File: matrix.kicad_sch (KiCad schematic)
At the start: 122 parts, among them SW1 esc, SW10 9, SW11 0, SW12 -, SW13 =, SW14 backspace, SW15 tab, SW16 q, SW17 w, SW18 e, SW19 r, SW2 1, SW20 t, SW21 y, SW22 u, SW23 i, SW24 o, SW25 p, SW26 [, SW27 ], SW28 \, SW29 capslock, SW3 2, SW30 a, SW31 s, SW32 d, SW33 f, SW34 g, SW35 h, SW36 j, SW37 k, SW38 l, SW39 ;, SW4 3, SW40 ', SW41 enter, SW42 lshift, SW43 z, SW44 x, SW45 c, SW46 v, SW47 b, SW48 n, SW49 m, SW5 4, SW50 ,, SW51 ., SW52 /, SW53 rshift, SW54 lctrl, SW55 lgui, SW56 lalt, SW57 space, SW58 ralt, SW59 rgui, SW6 5, SW60 fn, SW61 rctrl, SW7 6, SW8 7, SW9 8

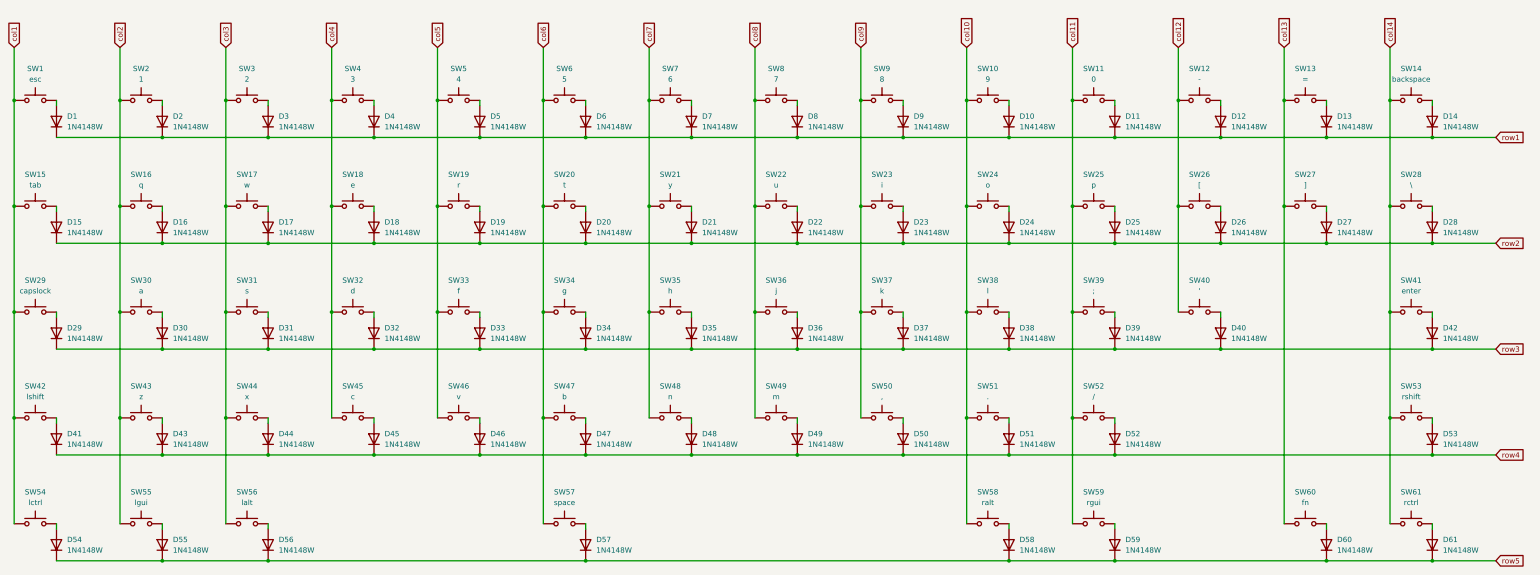
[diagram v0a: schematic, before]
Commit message: schema: rev0 done
Signed-off-by: HaoboGu <haobogu@outlook.com>
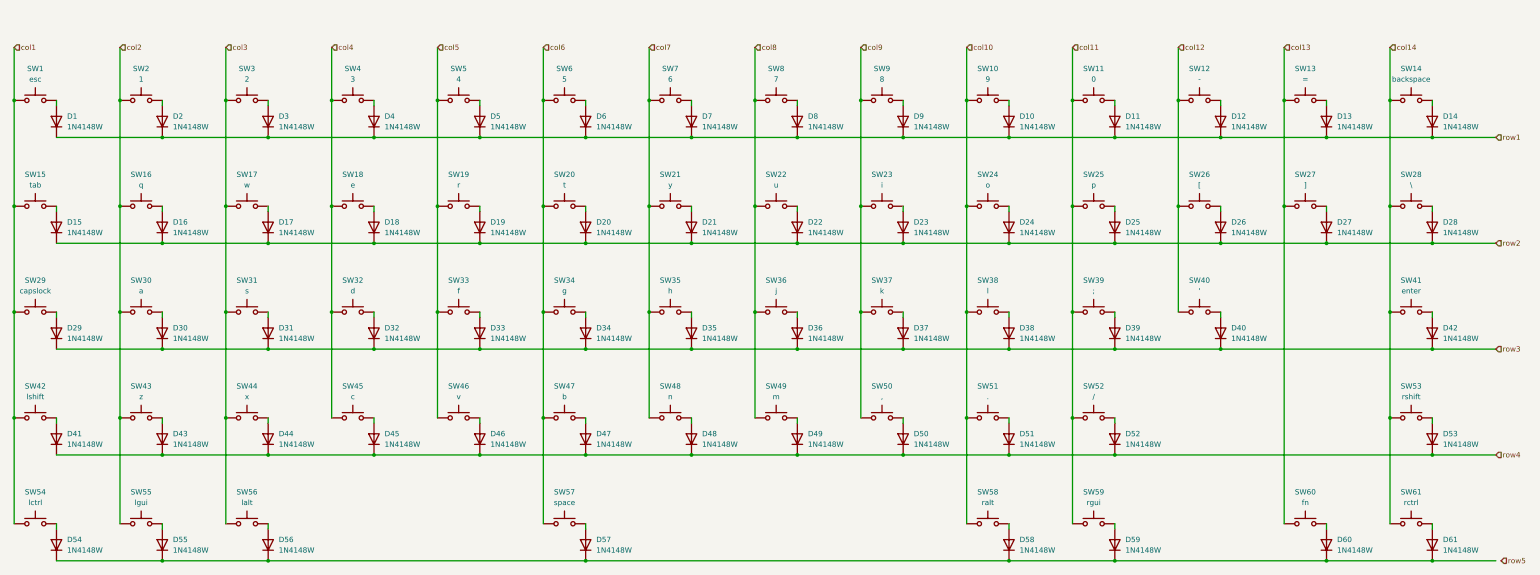
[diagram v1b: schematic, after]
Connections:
- net row5: no longer D54.1 (K), D55.1 (K), D56.1 (K), D57.1 (K), D58.1 (K), D59.1 (K), D60.1 (K), D61.1 (K)
- new net: D54.1 (K), D55.1 (K), D56.1 (K), D57.1 (K), D58.1 (K), D59.1 (K), D60.1 (K), D61.1 (K)

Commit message: assign footprints
Signed-off-by: HaoboGu <haobogu@outlook.com>
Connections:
- net row5: now also D54.1 (K), D55.1 (K), D56.1 (K), D57.1 (K), D58.1 (K), D59.1 (K), D60.1 (K), D61.1 (K)
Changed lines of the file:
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@@
 	(hierarchical_label "row5"
 		(shape input)
-		(at 382.27 186.69 0)
+		(at 381 186.69 0)
 		(fields_autoplaced yes)
 		(effects

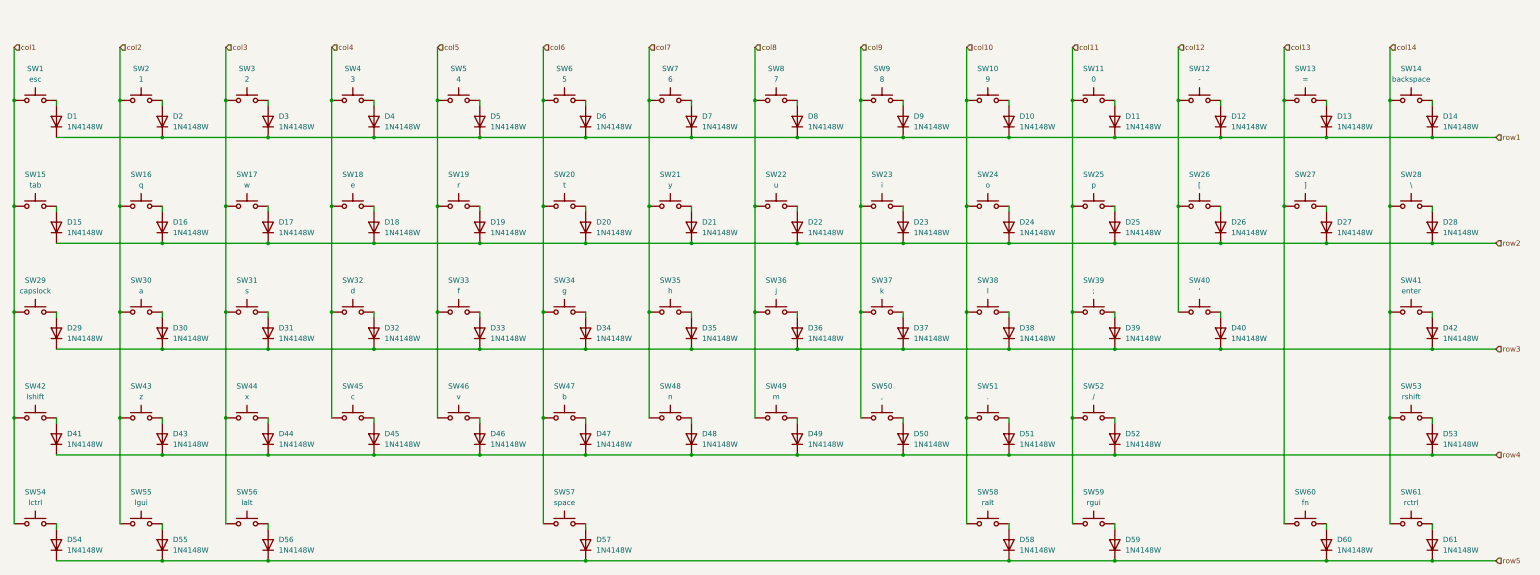
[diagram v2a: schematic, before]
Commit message: update battery socket
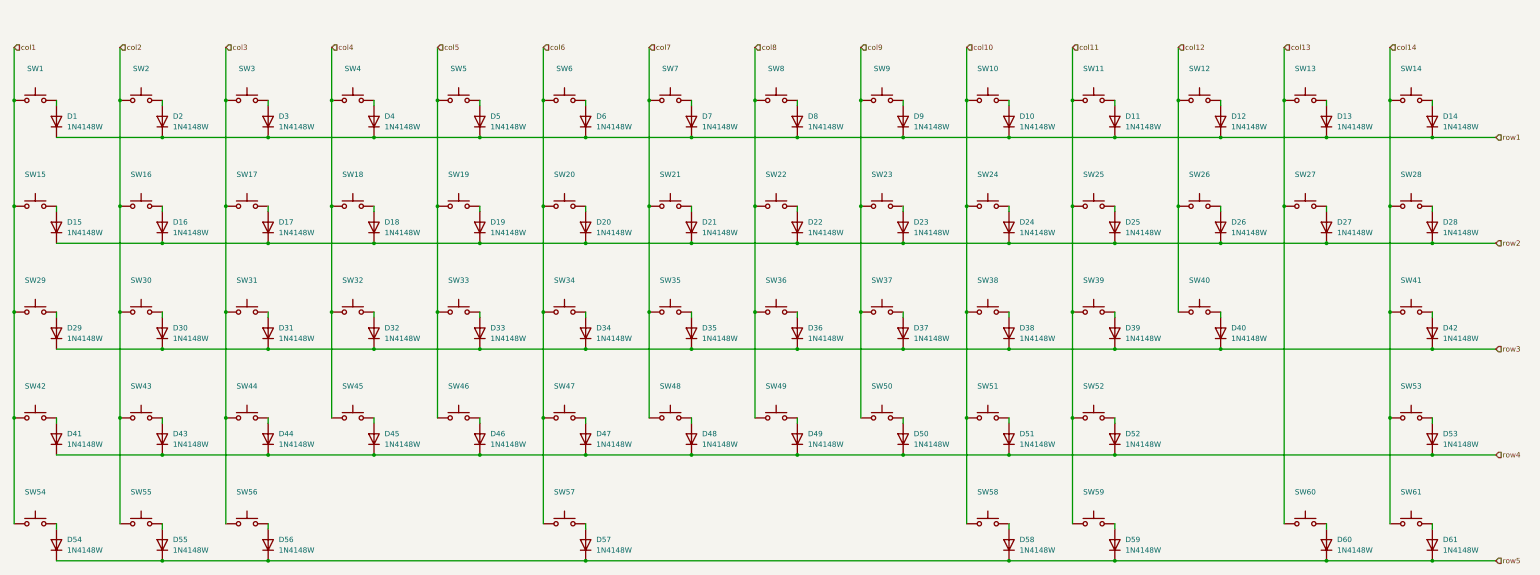
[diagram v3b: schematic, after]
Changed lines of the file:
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@@
 					(size 1.27 1.27)
 				)
+				(hide yes)
 			)
 		)
@@
 					(size 1.27 1.27)
 				)
+				(hide yes)
 			)
 		)
@@
 					(size 1.27 1.27)
 				)
+				(hide yes)
 			)
 		)
@@
 					(size 1.27 1.27)
 				)
+				(hide yes)
 			)
 		)
@@
 					(size 1.27 1.27)
 				)
+				(hide yes)
 			)
 		)
@@
 					(size 1.27 1.27)
 				)
+				(hide yes)
 			)
 		)
@@
 					(size 1.27 1.27)
 				)
+				(hide yes)
 			)
 		)
@@
 					(size 1.27 1.27)
 				)
+				(hide yes)
 			)
 		)
@@
 					(size 1.27 1.27)
 				)
+				(hide yes)
 			)
 		)
@@
 					(size 1.27 1.27)
 				)
+				(hide yes)
 			)
 		)
@@
 					(size 1.27 1.27)
 				)
+				(hide yes)
 			)
 		)
@@
 					(size 1.27 1.27)
 				)
+				(hide yes)
 			)
 		)
@@
 					(size 1.27 1.27)
 				)
+				(hide yes)
 			)
 		)
@@
 					(size 1.27 1.27)
 				)
+				(hide yes)
 			)
 		)
@@
 					(size 1.27 1.27)
 				)
+				(hide yes)
 			)
 		)
@@
 					(size 1.27 1.27)
 				)
+				(hide yes)
 			)
 		)
@@
 					(size 1.27 1.27)
 				)
+				(hide yes)
 			)
 		)
@@
 					(size 1.27 1.27)
 				)
+				(hide yes)
 			)
 		)
@@
 					(size 1.27 1.27)
 				)
+				(hide yes)
 			)
 		)
@@
 					(size 1.27 1.27)
 				)
+				(hide yes)
 			)
 		)
@@
 					(size 1.27 1.27)
 				)
+				(hide yes)
 			)
 		)
@@
 					(size 1.27 1.27)
 				)
+				(hide yes)
 			)
 		)
@@
 					(size 1.27 1.27)
 				)
+				(hide yes)
 			)
 		)
@@
 					(size 1.27 1.27)
 				)
+				(hide yes)
 			)
 		)
@@
 					(size 1.27 1.27)
 				)
+				(hide yes)
 			)
 		)
@@
 					(size 1.27 1.27)
 				)
+				(hide yes)
 			)
 		)
@@
 					(size 1.27 1.27)
 				)
+				(hide yes)
 			)
 		)
@@
 					(size 1.27 1.27)
 				)
+				(hide yes)
 			)
 		)
@@
 					(size 1.27 1.27)
 				)
+				(hide yes)
 			)
 		)
@@
 					(size 1.27 1.27)
 				)
+				(hide yes)
 			)
 		)
@@
 					(size 1.27 1.27)
 				)
+				(hide yes)
 			)
 		)
@@
 					(size 1.27 1.27)
 				)
+				(hide yes)
 			)
 		)
@@
 					(size 1.27 1.27)
 				)
+				(hide yes)
 			)
 		)
@@
 					(size 1.27 1.27)
 				)
+				(hide yes)
 			)
 		)
@@
 					(size 1.27 1.27)
 				)
+				(hide yes)
 			)
 		)
@@
 					(size 1.27 1.27)
 				)
+				(hide yes)
 			)
 		)
@@
 					(size 1.27 1.27)
 				)
+				(hide yes)
 			)
 		)
@@
 					(size 1.27 1.27)
 				)
+				(hide yes)
 			)
 		)
@@
 					(size 1.27 1.27)
 				)
+				(hide yes)
 			)
 		)
@@
 					(size 1.27 1.27)
 				)
+				(hide yes)
 			)
 		)
@@
 					(size 1.27 1.27)
 				)
+				(hide yes)
 			)
 		)
@@
 					(size 1.27 1.27)
 				)
+				(hide yes)
 			)
 		)
@@
 					(size 1.27 1.27)
 				)
+				(hide yes)
 			)
 		)
@@
 					(size 1.27 1.27)
 				)
+				(hide yes)
 			)
 		)
@@
 					(size 1.27 1.27)
 				)
+				(hide yes)
 			)
 		)
@@
 					(size 1.27 1.27)
 				)
+				(hide yes)
 			)
 		)
@@
 					(size 1.27 1.27)
 				)
+				(hide yes)
 			)
 		)
@@
 					(size 1.27 1.27)
 				)
+				(hide yes)
 			)
 		)
@@
 					(size 1.27 1.27)
 				)
+				(hide yes)
 			)
 		)
@@
 					(size 1.27 1.27)
 				)
+				(hide yes)
 			)
 		)
@@
 					(size 1.27 1.27)
 				)
+				(hide yes)
 			)
 		)
@@
 					(size 1.27 1.27)
 				)
+				(hide yes)
 			)
 		)
@@
 					(size 1.27 1.27)
 				)
+				(hide yes)
 			)
 		)
@@
 					(size 1.27 1.27)
 				)
+				(hide yes)
 			)
 		)
@@
 					(size 1.27 1.27)
 				)
+				(hide yes)
 			)
 		)
@@
 					(size 1.27 1.27)
 				)
+				(hide yes)
 			)
 		)
@@
 					(size 1.27 1.27)
 				)
+				(hide yes)
 			)
 		)
@@
 					(size 1.27 1.27)
 				)
+				(hide yes)
 			)
 		)
@@
 					(size 1.27 1.27)
 				)
+				(hide yes)
 			)
 		)
@@
 					(size 1.27 1.27)
 				)
+				(hide yes)
 			)
 		)
@@
 					(size 1.27 1.27)
 				)
+				(hide yes)
 			)
 		)
